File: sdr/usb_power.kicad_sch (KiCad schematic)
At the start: 7 parts, among them J1 USB_C_Receptacle_USB2.0

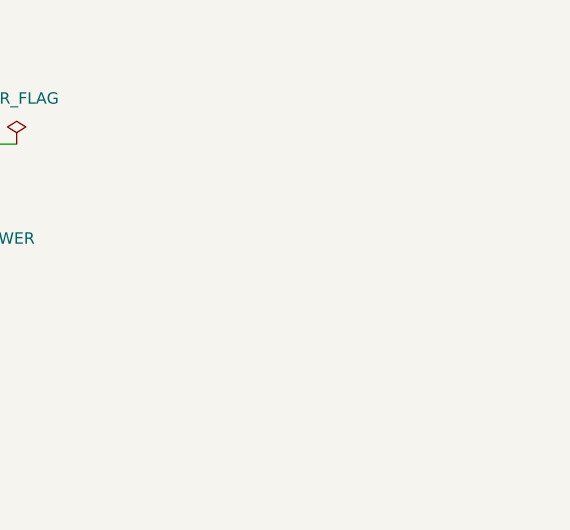
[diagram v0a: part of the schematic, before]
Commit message: Added 3.3V LDO and CPU sheet
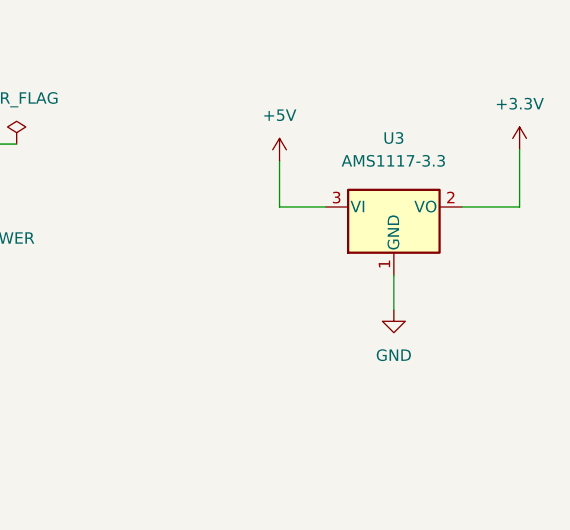
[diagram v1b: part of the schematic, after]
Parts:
- added U3: AMS1117-3.3, Package_TO_SOT_SMD:SOT-223-3_TabPin2, symbol Regulator_Linear:AMS1117-3.3
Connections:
- net +5V: now also U3.3 (VI)
- net GND: now also U3.1 (GND)
- new net +3.3V: U3.2 (VO)
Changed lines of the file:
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@@
+    (stroke (width 0) (type default) (color 0 0 0 0))
+  )
+  (wire (pts (xy 220.98 86.36) (xy 220.98 90.17))
+    (stroke (width 0) (type default) (color 0 0 0 0))
+  )
+  (wire (pts (xy 208.28 78.74) (xy 213.36 78.74))
     (stroke (width 0) (type default) (color 0 0 0 0))
   )
@@
     (stroke (width 0) (type default) (color 0 0 0 0))
   )
+  (wire (pts (xy 234.95 78.74) (xy 234.95 72.39))
+    (stroke (width 0) (type default) (color 0 0 0 0))
+  )
   (wire (pts (xy 156.21 71.755) (xy 160.655 71.755))
     (stroke (width 0) (type default) (color 0 0 0 0))
@@
     (stroke (width 0) (type default) (color 0 0 0 0))
   )
+  (wire (pts (xy 208.28 73.66) (xy 208.28 78.74))
+    (stroke (width 0) (type default) (color 0 0 0 0))
+  )
+  (wire (pts (xy 228.6 78.74) (xy 234.95 78.74))
+    (stroke (width 0) (type default) (color 0 0 0 0))
+  )
   (wire (pts (xy 148.59 88.265) (xy 148.59 89.535))
     (stroke (width 0) (type default) (color 0 0 0 0))
@@
   (wire (pts (xy 120.015 112.395) (xy 120.015 115.57))
     (stroke (width 0) (type default) (color 0 0 0 0))
+  )
+  (symbol (lib_id "Regulator_Linear:AMS1117-3.3") (at 220.98 78.74 0) (unit 1)
+    (in_bom yes) (on_board yes) (fields_autoplaced)
+    (property "Reference" "U3" (id 0) (at 220.98 71.12 0))
+    (property "Value" "AMS1117-3.3" (id 1) (at 220.98 73.66 0))
+    (property "Footprint" "Package_TO_SOT_SMD:SOT-223-3_TabPin2" (id 2) (at 220.98 73.66 0)
+      (effects (font (size 1.27 1.27)) hide)
+    )
+    (property "Datasheet" "http://www.advanced-monolithic.com/pdf/ds1117.pdf" (id 3) (at 223.52 85.09 0)
+      (effects (font (size 1.27 1.27)) hide)
+    )
+    (property "LCSC" "C6186" (id 4) (at 220.98 78.74 0)
+      (effects (font (size 1.27 1.27)) hide)
+    )
+    (pin "1")
+    (pin "2")
+    (pin "3")
   )
   (symbol (lib_id "Connector:USB_C_Receptacle_USB2.0") (at 123.825 86.995 0) (unit 1)
@@
     (pin "1")
   )
+  (symbol (lib_name "+5V_1") (lib_id "power:+5V") (at 208.28 73.66 0) (unit 1)
+    (in_bom yes) (on_board yes) (fields_autoplaced)
+    (property "Reference" "#PWR015" (id 0) (at 208.28 77.47 0)
+      (effects (font (size 1.27 1.27)) hide)
+    )
+    (property "Value" "+5V" (id 1) (at 208.28 68.58 0))
+    (property "Footprint" "" (id 2) (at 208.28 73.66 0)
+      (effects (font (size 1.27 1.27)) hide)
+    )
+    (property "Datasheet" "" (id 3) (at 208.28 73.66 0)
+      (effects (font (size 1.27 1.27)) hide)
+    )
+    (pin "1")
+  )
   (symbol (lib_id "Device:R") (at 170.815 90.805 0) (unit 1)
     (in_bom yes) (on_board yes) (fields_autoplaced)
@@
     (pin "1")
     (pin "2")
+  )
+  (symbol (lib_id "power:GND") (at 220.98 90.17 0) (unit 1)
+    (in_bom yes) (on_board yes) (fields_autoplaced)
+    (property "Reference" "#PWR016" (id 0) (at 220.98 96.52 0)
+      (effects (font (size 1.27 1.27)) hide)
+    )
+    (property "Value" "GND" (id 1) (at 220.98 95.25 0))
+    (property "Footprint" "" (id 2) (at 220.98 90.17 0)
+      (effects (font (size 1.27 1.27)) hide)
+    )
+    (property "Datasheet" "" (id 3) (at 220.98 90.17 0)
+      (effects (font (size 1.27 1.27)) hide)
+    )
+    (property "JLCPCB" "C2296" (id 4) (at 220.98 90.17 0)
+      (effects (font (size 1.27 1.27)) hide)
+    )
+    (pin "1")
   )
   (symbol (lib_id "Device:LED") (at 170.815 79.375 90) (unit 1)
@@
       (effects (font (size 1.27 1.27)) hide)
     )
+    (pin "1")
+  )
+  (symbol (lib_id "power:+3.3V") (at 234.95 72.39 0) (unit 1)
+    (in_bom yes) (on_board yes) (fields_autoplaced)
+    (property "Reference" "#PWR017" (id 0) (at 234.95 76.2 0)
+      (effects (font (size 1.27 1.27)) hide)
+    )
+    (property "Value" "+3.3V" (id 1) (at 234.95 67.31 0))
+    (property "Footprint" "" (id 2) (at 234.95 72.39 0)
+      (effects (font (size 1.27 1.27)) hide)
+    )
+    (property "Datasheet" "" (id 3) (at 234.95 72.39 0)
+      (effects (font (size 1.27 1.27)) hide)
+    )

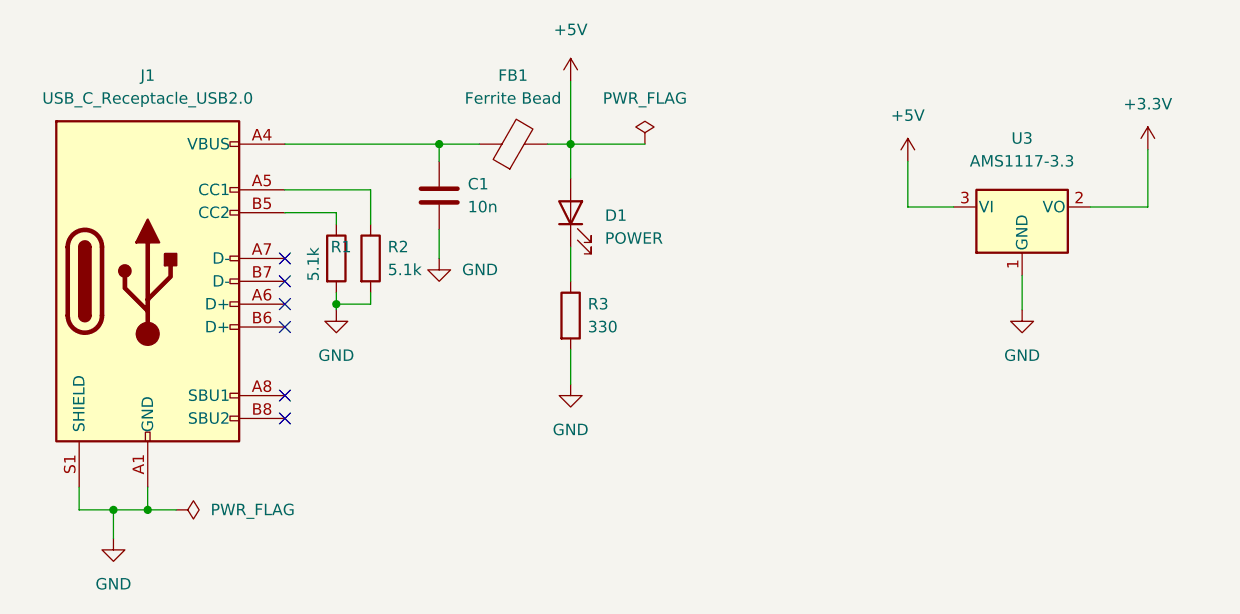
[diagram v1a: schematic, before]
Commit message: Update lots of things. Now have basic CPU as well as some crude mixers
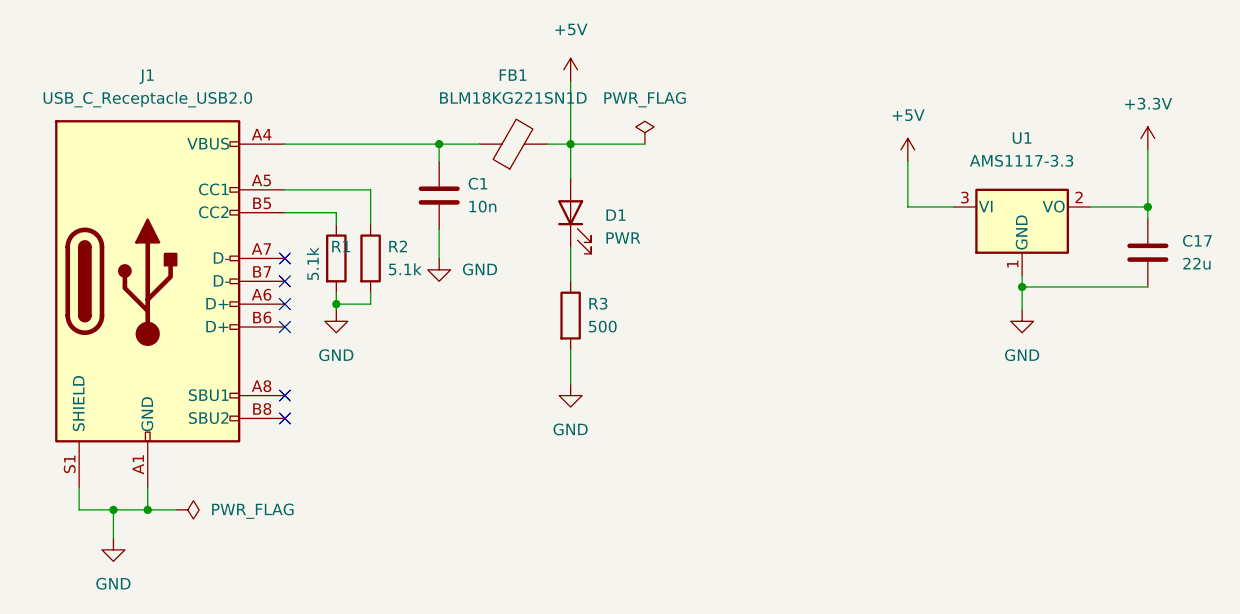
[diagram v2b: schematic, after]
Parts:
- added C17: 22u, Capacitor_SMD:C_1206_3216Metric, symbol Device:C
- D1: value POWER -> PWR
- FB1: value Ferrite Bead -> BLM18KG221SN1D
- R3: value 330 -> 500; LCSC C22962 -> (none)
- renumbered U3 to U1
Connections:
- net +3.3V: now also C17.1
- net GND: now also C17.2
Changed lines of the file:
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@@
   (junction (at 170.815 71.755) (diameter 0) (color 0 0 0 0)
   )
+  (junction (at 234.95 78.74) (diameter 0) (color 0 0 0 0)
+  )
   (junction (at 120.015 112.395) (diameter 0) (color 0 0 0 0)
   )
@@
   )
   (junction (at 156.21 71.755) (diameter 0) (color 0 0 0 0)
+  )
+  (junction (at 220.98 87.63) (diameter 0) (color 0 0 0 0)
   )
   (no_connect (at 139.065 102.235))
@@
     (stroke (width 0) (type default) (color 0 0 0 0))
   )
+  (wire (pts (xy 234.95 78.74) (xy 234.95 80.01))
+    (stroke (width 0) (type default) (color 0 0 0 0))
+  )
   (wire (pts (xy 168.275 71.755) (xy 170.815 71.755))
     (stroke (width 0) (type default) (color 0 0 0 0))
@@
     (stroke (width 0) (type default) (color 0 0 0 0))
   )
-  (wire (pts (xy 220.98 86.36) (xy 220.98 90.17))
+  (wire (pts (xy 220.98 86.36) (xy 220.98 87.63))
     (stroke (width 0) (type default) (color 0 0 0 0))
   )
@@
     (stroke (width 0) (type default) (color 0 0 0 0))
   )
+  (wire (pts (xy 220.98 87.63) (xy 234.95 87.63))
+    (stroke (width 0) (type default) (color 0 0 0 0))
+  )
   (wire (pts (xy 234.95 78.74) (xy 234.95 72.39))
     (stroke (width 0) (type default) (color 0 0 0 0))
@@
     (stroke (width 0) (type default) (color 0 0 0 0))
   )
+  (wire (pts (xy 220.98 87.63) (xy 220.98 90.17))
+    (stroke (width 0) (type default) (color 0 0 0 0))
+  )
   (symbol (lib_id "Regulator_Linear:AMS1117-3.3") (at 220.98 78.74 0) (unit 1)
     (in_bom yes) (on_board yes) (fields_autoplaced)
-    (property "Reference" "U3" (id 0) (at 220.98 71.12 0))
+    (property "Reference" "U1" (id 0) (at 220.98 71.12 0))
     (property "Value" "AMS1117-3.3" (id 1) (at 220.98 73.66 0))
     (property "Footprint" "Package_TO_SOT_SMD:SOT-223-3_TabPin2" (id 2) (at 220.98 73.66 0)
@@
     (pin "2")
     (pin "3")
+  )
+  (symbol (lib_id "Device:C") (at 234.95 83.82 0) (unit 1)
+    (in_bom yes) (on_board yes) (fields_autoplaced)
+    (property "Reference" "C17" (id 0) (at 238.76 82.5499 0)
+      (effects (font (size 1.27 1.27)) (justify left))
+    )
+    (property "Value" "22u" (id 1) (at 238.76 85.0899 0)
+      (effects (font (size 1.27 1.27)) (justify left))
+    )
+    (property "Footprint" "Capacitor_SMD:C_1206_3216Metric" (id 2) (at 235.9152 87.63 0)
+      (effects (font (size 1.27 1.27)) hide)
+    )
+    (property "Datasheet" "~" (id 3) (at 234.95 83.82 0)
+      (effects (font (size 1.27 1.27)) hide)
+    )
+    (pin "1")
+    (pin "2")
   )
   (symbol (lib_id "Connector:USB_C_Receptacle_USB2.0") (at 123.825 86.995 0) (unit 1)
@@
   (symbol (lib_name "+5V_1") (lib_id "power:+5V") (at 208.28 73.66 0) (unit 1)
     (in_bom yes) (on_board yes) (fields_autoplaced)
-    (property "Reference" "#PWR015" (id 0) (at 208.28 77.47 0)
+    (property "Reference" "#PWR06" (id 0) (at 208.28 77.47 0)
       (effects (font (size 1.27 1.27)) hide)
     )
@@
       (effects (font (size 1.27 1.27)) (justify left))
     )
-    (property "Value" "330" (id 1) (at 172.72 92.0749 0)
+    (property "Value" "500" (id 1) (at 172.72 92.0749 0)
       (effects (font (size 1.27 1.27)) (justify left))
     )
@@
       (effects (font (size 1.27 1.27)) hide)
     )
-    (property "LCSC" "C22962" (id 4) (at 173.355 89.5349 0)
-      (effects (font (size 1.27 1.27)) hide)
-    )
     (pin "1")
     (pin "2")
@@
   (symbol (lib_id "power:GND") (at 220.98 90.17 0) (unit 1)
     (in_bom yes) (on_board yes) (fields_autoplaced)
-    (property "Reference" "#PWR016" (id 0) (at 220.98 96.52 0)
+    (property "Reference" "#PWR07" (id 0) (at 220.98 96.52 0)
       (effects (font (size 1.27 1.27)) hide)
     )
@@
       (effects (font (size 1.27 1.27)) (justify right))
     )
-    (property "Value" "POWER" (id 1) (at 174.625 82.2324 90)
+    (property "Value" "PWR" (id 1) (at 174.625 82.2324 90)
       (effects (font (size 1.27 1.27)) (justify right))
     )
@@
   (symbol (lib_id "power:+3.3V") (at 234.95 72.39 0) (unit 1)
     (in_bom yes) (on_board yes) (fields_autoplaced)
-    (property "Reference" "#PWR017" (id 0) (at 234.95 76.2 0)
+    (property "Reference" "#PWR08" (id 0) (at 234.95 76.2 0)
       (effects (font (size 1.27 1.27)) hide)
     )
@@
     (in_bom yes) (on_board yes)
     (property "Reference" "FB1" (id 0) (at 164.4142 64.135 90))
-    (property "Value" "Ferrite Bead" (id 1) (at 164.4142 66.675 90))
+    (property "Value" "BLM18KG221SN1D" (id 1) (at 164.4142 66.675 90))
     (property "Footprint" "Inductor_SMD:L_0603_1608Metric" (id 2) (at 164.465 73.533 90)
       (effects (font (size 1.27 1.27)) hide)

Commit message: Added ST-link 6-pin 0.1 programming header
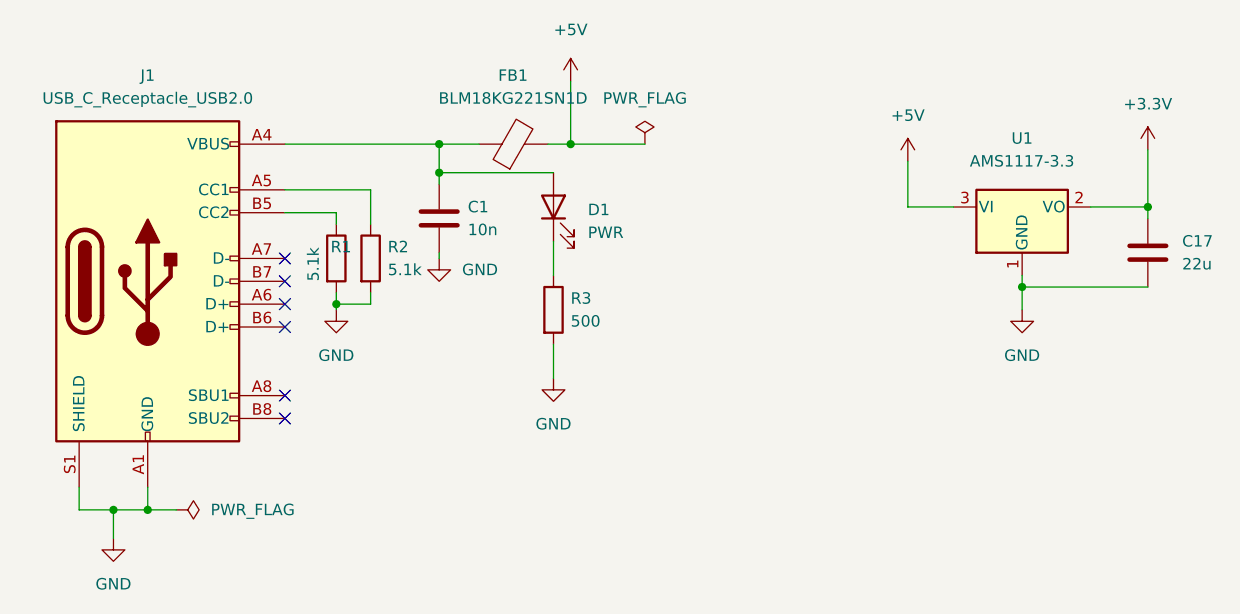
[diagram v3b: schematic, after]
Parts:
- R1, R2: footprint Resistor_SMD:R_0402_1005Metric -> Resistor_SMD:R_0603_1608Metric
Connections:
- net +5V: no longer D1.2 (A)
- net at C1.1, FB1.1, J1.A4 (VBUS)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: now also D1.2 (A)
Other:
- moved on the sheet: C1, D1, R3
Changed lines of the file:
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@@
 (kicad_sch (version 20211123) (generator eeschema)
   (paper "A4")
+  (junction (at 156.21 74.93) (diameter 0) (color 0 0 0 0)
+  )
   (junction (at 144.78 89.535) (diameter 0) (color 0 0 0 0)
   )
@@
     (stroke (width 0) (type default) (color 0 0 0 0))
   )
-  (wire (pts (xy 156.21 81.28) (xy 156.21 84.455))
+  (wire (pts (xy 156.21 83.82) (xy 156.21 84.455))
     (stroke (width 0) (type default) (color 0 0 0 0))
   )
@@
     (stroke (width 0) (type default) (color 0 0 0 0))
   )
+  (wire (pts (xy 156.21 74.93) (xy 168.91 74.93))
+    (stroke (width 0) (type default) (color 0 0 0 0))
+  )
   (wire (pts (xy 144.78 89.535) (xy 144.78 90.17))
     (stroke (width 0) (type default) (color 0 0 0 0))
   )
-  (wire (pts (xy 170.815 83.185) (xy 170.815 86.995))
+  (wire (pts (xy 168.91 82.55) (xy 168.91 86.36))
     (stroke (width 0) (type default) (color 0 0 0 0))
   )
@@
     (stroke (width 0) (type default) (color 0 0 0 0))
   )
-  (wire (pts (xy 170.815 71.755) (xy 170.815 75.565))
+  (wire (pts (xy 156.21 74.93) (xy 156.21 76.2))
     (stroke (width 0) (type default) (color 0 0 0 0))
   )
@@
     (stroke (width 0) (type default) (color 0 0 0 0))
   )
-  (wire (pts (xy 170.815 94.615) (xy 170.815 98.425))
+  (wire (pts (xy 168.91 93.98) (xy 168.91 97.79))
     (stroke (width 0) (type default) (color 0 0 0 0))
   )
@@
     (stroke (width 0) (type default) (color 0 0 0 0))
   )
-  (wire (pts (xy 156.21 71.755) (xy 156.21 73.66))
+  (wire (pts (xy 156.21 71.755) (xy 156.21 74.93))
     (stroke (width 0) (type default) (color 0 0 0 0))
   )
@@
     (pin "1")
   )
-  (symbol (lib_id "Device:R") (at 170.815 90.805 0) (unit 1)
-    (in_bom yes) (on_board yes) (fields_autoplaced)
-    (property "Reference" "R3" (id 0) (at 172.72 89.5349 0)
-      (effects (font (size 1.27 1.27)) (justify left))
-    )
-    (property "Value" "500" (id 1) (at 172.72 92.0749 0)
-      (effects (font (size 1.27 1.27)) (justify left))
-    )
-    (property "Footprint" "Resistor_SMD:R_0402_1005Metric" (id 2) (at 169.037 90.805 90)
-      (effects (font (size 1.27 1.27)) hide)
-    )
-    (property "Datasheet" "~" (id 3) (at 170.815 90.805 0)
+  (symbol (lib_id "Device:R") (at 168.91 90.17 0) (unit 1)
+    (in_bom yes) (on_board yes) (fields_autoplaced)
+    (property "Reference" "R3" (id 0) (at 170.815 88.8999 0)
+      (effects (font (size 1.27 1.27)) (justify left))
+    )
+    (property "Value" "500" (id 1) (at 170.815 91.4399 0)
+      (effects (font (size 1.27 1.27)) (justify left))
+    )
+    (property "Footprint" "Resistor_SMD:R_0402_1005Metric" (id 2) (at 167.132 90.17 90)
+      (effects (font (size 1.27 1.27)) hide)
+    )
+    (property "Datasheet" "~" (id 3) (at 168.91 90.17 0)
       (effects (font (size 1.27 1.27)) hide)
     )
@@
       (effects (font (size 1.27 1.27)) (justify left))
     )
-    (property "Footprint" "Resistor_SMD:R_0402_1005Metric" (id 2) (at 146.812 84.455 90)
+    (property "Footprint" "Resistor_SMD:R_0603_1608Metric" (id 2) (at 146.812 84.455 90)
       (effects (font (size 1.27 1.27)) hide)
     )
@@
     (pin "1")
   )
-  (symbol (lib_id "Device:LED") (at 170.815 79.375 90) (unit 1)
-    (in_bom yes) (on_board yes) (fields_autoplaced)
-    (property "Reference" "D1" (id 0) (at 174.625 79.6924 90)
+  (symbol (lib_id "Device:LED") (at 168.91 78.74 90) (unit 1)
+    (in_bom yes) (on_board yes) (fields_autoplaced)
+    (property "Reference" "D1" (id 0) (at 172.72 79.0574 90)
       (effects (font (size 1.27 1.27)) (justify right))
     )
-    (property "Value" "PWR" (id 1) (at 174.625 82.2324 90)
+    (property "Value" "PWR" (id 1) (at 172.72 81.5974 90)
       (effects (font (size 1.27 1.27)) (justify right))
     )
-    (property "Footprint" "Diode_SMD:D_0603_1608Metric" (id 2) (at 170.815 79.375 0)
-      (effects (font (size 1.27 1.27)) hide)
-    )
-    (property "Datasheet" "~" (id 3) (at 170.815 79.375 0)
-      (effects (font (size 1.27 1.27)) hide)
-    )
-    (property "LCSC" "C72043" (id 4) (at 170.815 79.375 90)
+    (property "Footprint" "Diode_SMD:D_0603_1608Metric" (id 2) (at 168.91 78.74 0)
+      (effects (font (size 1.27 1.27)) hide)
+    )
+    (property "Datasheet" "~" (id 3) (at 168.91 78.74 0)
+      (effects (font (size 1.27 1.27)) hide)
+    )
+    (property "LCSC" "C72043" (id 4) (at 168.91 78.74 90)
       (effects (font (size 1.27 1.27)) hide)
     )
@@
       (effects (font (size 1.27 1.27)) (justify left))
     )
-    (property "Footprint" "Resistor_SMD:R_0402_1005Metric" (id 2) (at 143.002 84.455 90)
+    (property "Footprint" "Resistor_SMD:R_0603_1608Metric" (id 2) (at 143.002 84.455 90)
       (effects (font (size 1.27 1.27)) hide)
     )
@@
     (pin "1")
   )
-  (symbol (lib_id "power:GND") (at 170.815 98.425 0) (unit 1)
-    (in_bom yes) (on_board yes) (fields_autoplaced)
-    (property "Reference" "#PWR05" (id 0) (at 170.815 104.775 0)
-      (effects (font (size 1.27 1.27)) hide)
-    )
-    (property "Value" "GND" (id 1) (at 170.815 103.505 0))
-    (property "Footprint" "" (id 2) (at 170.815 98.425 0)
-      (effects (font (size 1.27 1.27)) hide)
-    )
-    (property "Datasheet" "" (id 3) (at 170.815 98.425 0)
-      (effects (font (size 1.27 1.27)) hide)
-    )
-    (property "JLCPCB" "C2296" (id 4) (at 170.815 98.425 0)
+  (symbol (lib_id "power:GND") (at 168.91 97.79 0) (unit 1)
+    (in_bom yes) (on_board yes) (fields_autoplaced)
+    (property "Reference" "#PWR05" (id 0) (at 168.91 104.14 0)
+      (effects (font (size 1.27 1.27)) hide)
+    )
+    (property "Value" "GND" (id 1) (at 168.91 102.87 0))
+    (property "Footprint" "" (id 2) (at 168.91 97.79 0)
+      (effects (font (size 1.27 1.27)) hide)
+    )
+    (property "Datasheet" "" (id 3) (at 168.91 97.79 0)
+      (effects (font (size 1.27 1.27)) hide)
+    )
+    (property "JLCPCB" "C2296" (id 4) (at 168.91 97.79 0)
       (effects (font (size 1.27 1.27)) hide)
     )
@@
     (pin "1")
   )
-  (symbol (lib_id "Device:C") (at 156.21 77.47 0) (unit 1)
-    (in_bom yes) (on_board yes) (fields_autoplaced)
-    (property "Reference" "C1" (id 0) (at 159.385 76.1999 0)
-      (effects (font (size 1.27 1.27)) (justify left))
-    )
-    (property "Value" "10n" (id 1) (at 159.385 78.7399 0)
-      (effects (font (size 1.27 1.27)) (justify left))
-    )
-    (property "Footprint" "Capacitor_SMD:C_0603_1608Metric" (id 2) (at 157.1752 81.28 0)
-      (effects (font (size 1.27 1.27)) hide)
-    )
-    (property "Datasheet" "~" (id 3) (at 156.21 77.47 0)
-      (effects (font (size 1.27 1.27)) hide)
-    )
-    (property "LCSC" "C57112" (id 4) (at 159.385 76.1999 0)
-      (effects (font (size 1.27 1.27)) hide)
-    )
+  (symbol (lib_id "Device:C") (at 156.21 80.01 0) (unit 1)
+    (in_bom yes) (on_board yes) (fields_autoplaced)
+    (property "Reference" "C1" (id 0) (at 159.385 78.7399 0)
+      (effects (font (size 1.27 1.27)) (justify left))
+    )
+    (property "Value" "10n" (id 1) (at 159.385 81.2799 0)
+      (effects (font (size 1.27 1.27)) (justify left))
+    )
+    (property "Footprint" "Capacitor_SMD:C_0603_1608Metric" (id 2) (at 157.1752 83.82 0)
+      (effects (font (size 1.27 1.27)) hide)
+    )
+    (property "Datasheet" "~" (id 3) (at 156.21 80.01 0)
+      (effects (font (size 1.27 1.27)) hide)
+    )
+    (property "LCSC" "C57112" (id 4) (at 159.385 78.7399 0)
+      (effects (font (size 1.27 1.27)) hide)
+    )
